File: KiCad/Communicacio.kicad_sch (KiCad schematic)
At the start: 0 parts

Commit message: Procesament i comunicació
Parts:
- added C7: 100nF, symbol Device:C
- added J2: USB_B_Micro, symbol Connector:USB_B_Micro
- added R11: 10K, symbol Device:R
- added U5: FT232RL, Package_SO:SSOP-28_5.3x10.2mm_P0.65mm, symbol Interface_USB:FT232RL
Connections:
- new net: J2.2 (D-), U5.16 (USBD-)
- new net: J2.3 (D+), U5.15 (USBD+)
- new net: C7.2, U5.17 (3V3OUT)
- new net: R11.2, U5.19 (~{RESET})
- new net GND: C7.1, J2.5 (GND), J2.6 (Shield), U5.18 (GND), U5.21 (GND), U5.25 (AGND), U5.26 (TEST), U5.7 (GND)
- new net GPIO: U5.10 (DCD), U5.11 (CTS), U5.2 (DTR), U5.3 (RTS), U5.6 (RI), U5.9 (DCR)
- new net U1RX: U5.1 (TXD)
- new net U1TX: U5.5 (RXD)
- new net VCC: J2.1 (VBUS), R11.1, U5.20 (VCC), U5.4 (VCCIO)
- no-connect marks 0 -> 8
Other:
- note added: "USART"

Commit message: botonera, datashet usart
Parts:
- added C8: 100 nF, symbol Device:C
- added SW2, SW3, SW4, SW5, SW6: SW_SPDT, symbol Switch:SW_SPDT
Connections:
- net GND: now also C8.1, SW2.1 (A), SW3.1 (A), SW4.1 (A), SW5.1 (A), SW6.1 (A)
- net VCC: now also C8.2, SW2.2 (B), SW3.2 (B), SW4.2 (B), SW5.2 (B), SW6.2 (B); no longer J2.1 (VBUS), U5.20 (VCC)
- new net IN_CA: SW4.3 (C)
- new net IN_CR: SW5.3 (C)
- new net IN_L: SW2.3 (C)
- new net IN_LF: SW6.3 (C)
- new net IN_R: SW3.3 (C)
- new net VCC_5: J2.1 (VBUS), U5.20 (VCC)
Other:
- note added: "BOTONERA"

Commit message: Programador
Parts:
- added J3: Conn_PIC_ICSP_ICD, symbol Connector:Conn_PIC_ICSP_ICD
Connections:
- net GND: now also J3.3 (VSS)
- net VCC: now also J3.2 (VDD)
- new net MCLR: J3.1 (~{MCLR}/VPP)
- new net PGC: J3.5 (PGC/ICSPCLK)
- new net PGD: J3.4 (PGD/ICSPDAT)
- no-connect marks 8 -> 9
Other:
- note added: "PROGRAMACIÓ"

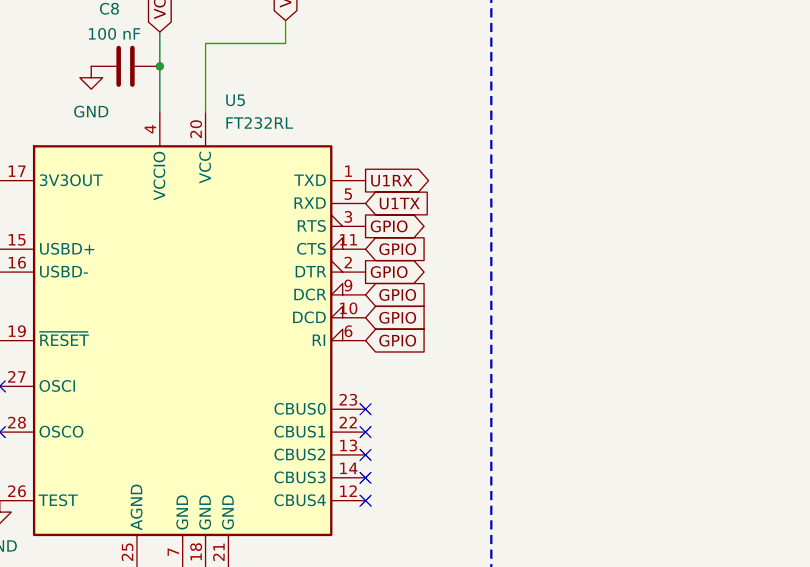
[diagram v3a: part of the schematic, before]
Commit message: acabar can, estil y micro biel
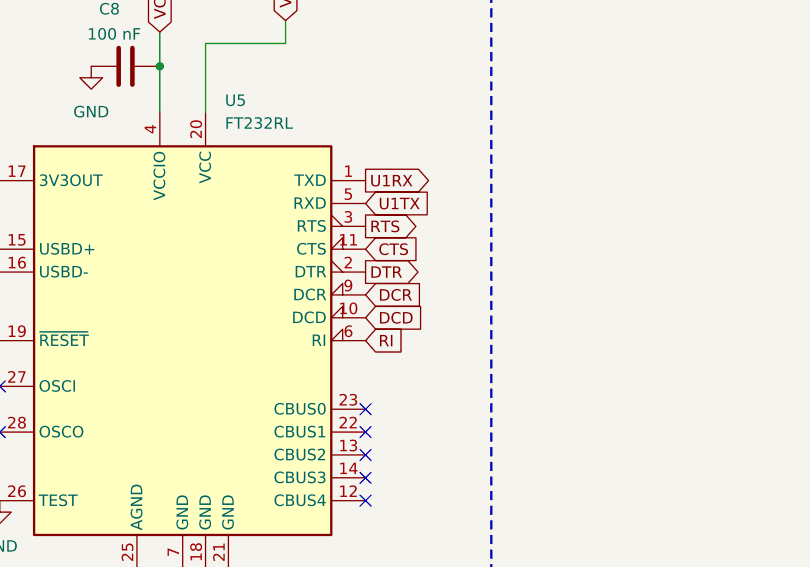
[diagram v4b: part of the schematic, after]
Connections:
- removed net GPIO: U5.10 (DCD), U5.11 (CTS), U5.2 (DTR), U5.3 (RTS), U5.6 (RI), U5.9 (DCR)
- new net CTS: U5.11 (CTS)
- new net DCD: U5.10 (DCD)
- new net DCR: U5.9 (DCR)
- new net DTR: U5.2 (DTR)
- new net RI: U5.6 (RI)
- new net RTS: U5.3 (RTS)
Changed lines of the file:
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@@
 		)
 	)
-	(global_label "GPIO"
+	(global_label "DTR"
 		(shape output)
 		(at 121.92 64.77 0)
@@
 		)
 		(property "Intersheetrefs" "${INTERSHEET_REFS}"
-			(at 129.3805 64.77 0)
+			(at 128.4128 64.77 0)
 			(effects
 				(font
@@
 		)
 	)
-	(global_label "GPIO"
+	(global_label "CTS"
 		(shape input)
 		(at 121.92 62.23 0)
@@
 		)
 		(property "Intersheetrefs" "${INTERSHEET_REFS}"
-			(at 129.3805 62.23 0)
+			(at 128.3523 62.23 0)
 			(effects
 				(font
@@
 		)
 	)
-	(global_label "GPIO"
+	(global_label "DCD"
 		(shape input)
 		(at 121.92 69.85 0)
@@
 		)
 		(property "Intersheetrefs" "${INTERSHEET_REFS}"
-			(at 129.3805 69.85 0)
-			(effects
-				(font
-					(size 1.27 1.27)
-				)
-				(justify left)
-				(hide yes)
-			)
-		)
-	)
-	(global_label "GPIO"
+			(at 128.7152 69.85 0)
+			(effects
+				(font
+					(size 1.27 1.27)
+				)
+				(justify left)
+				(hide yes)
+			)
+		)
+	)
+	(global_label "DCR"
 		(shape input)
 		(at 121.92 67.31 0)
@@
 		)
 		(property "Intersheetrefs" "${INTERSHEET_REFS}"
-			(at 129.3805 67.31 0)
+			(at 128.7152 67.31 0)
 			(effects
 				(font
@@
 		)
 	)
-	(global_label "GPIO"
+	(global_label "RI"
 		(shape input)
 		(at 121.92 72.39 0)
@@
 		)
 		(property "Intersheetrefs" "${INTERSHEET_REFS}"
-			(at 129.3805 72.39 0)
+			(at 126.78 72.39 0)
 			(effects
 				(font
@@
 		)
 	)
-	(global_label "GPIO"
+	(global_label "RTS"
 		(shape output)
 		(at 121.92 59.69 0)
@@
 		)
 		(property "Intersheetrefs" "${INTERSHEET_REFS}"
-			(at 129.3805 59.69 0)
-			(effects
-				(font
+			(at 128.3523 59.69 0)
+			(effects
+				(font

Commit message: Debugging
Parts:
- removed J2: USB_B_Micro, symbol Connector:USB_B_Micro
- removed J3: Conn_PIC_ICSP_ICD, symbol Connector:Conn_PIC_ICSP_ICD
- added J5: DE9_Pins, symbol Connector:DE9_Pins
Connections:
- net GND: now also J5.2
- net IN_CA: now also SW4.2 (B); no longer SW4.3 (C)
- net IN_CR: now also SW5.2 (B); no longer SW5.3 (C)
- net IN_L: now also SW2.2 (B); no longer SW2.3 (C)
- net IN_LF: now also SW6.2 (B); no longer SW6.3 (C)
- net IN_R: now also SW3.2 (B); no longer SW3.3 (C)
- net VCC: now also SW2.3 (C), SW3.3 (C), SW4.3 (C), SW5.3 (C), SW6.3 (C); no longer SW2.2 (B), SW3.2 (B), SW4.2 (B), SW5.2 (B), SW6.2 (B)
- net at U5.16 (USBD-): now also J5.3
- net at U5.15 (USBD+): now also J5.4
- no-connect marks 9 -> 13
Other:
- note removed: "PROGRAMACIÓ"

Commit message: titulos
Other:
- title: (none) -> Communicacio
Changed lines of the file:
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@@
 	(paper "A4")
 	(title_block
+		(title "Communicacio")
 		(date "2026-03-16")
 	)
